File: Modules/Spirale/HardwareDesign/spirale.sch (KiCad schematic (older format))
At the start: 1 part

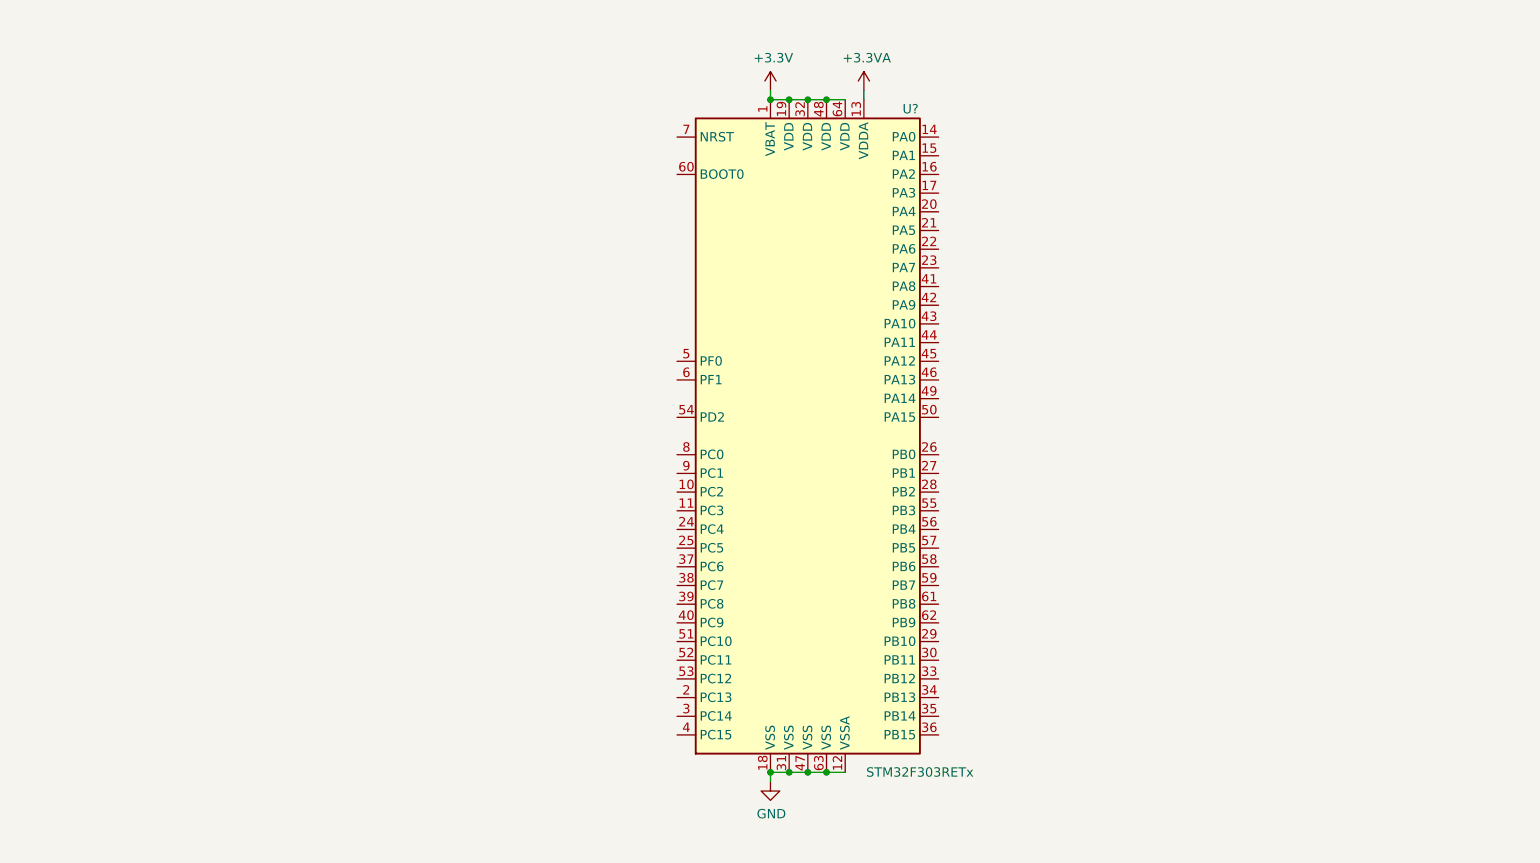
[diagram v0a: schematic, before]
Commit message: hw: add most of the needed nets
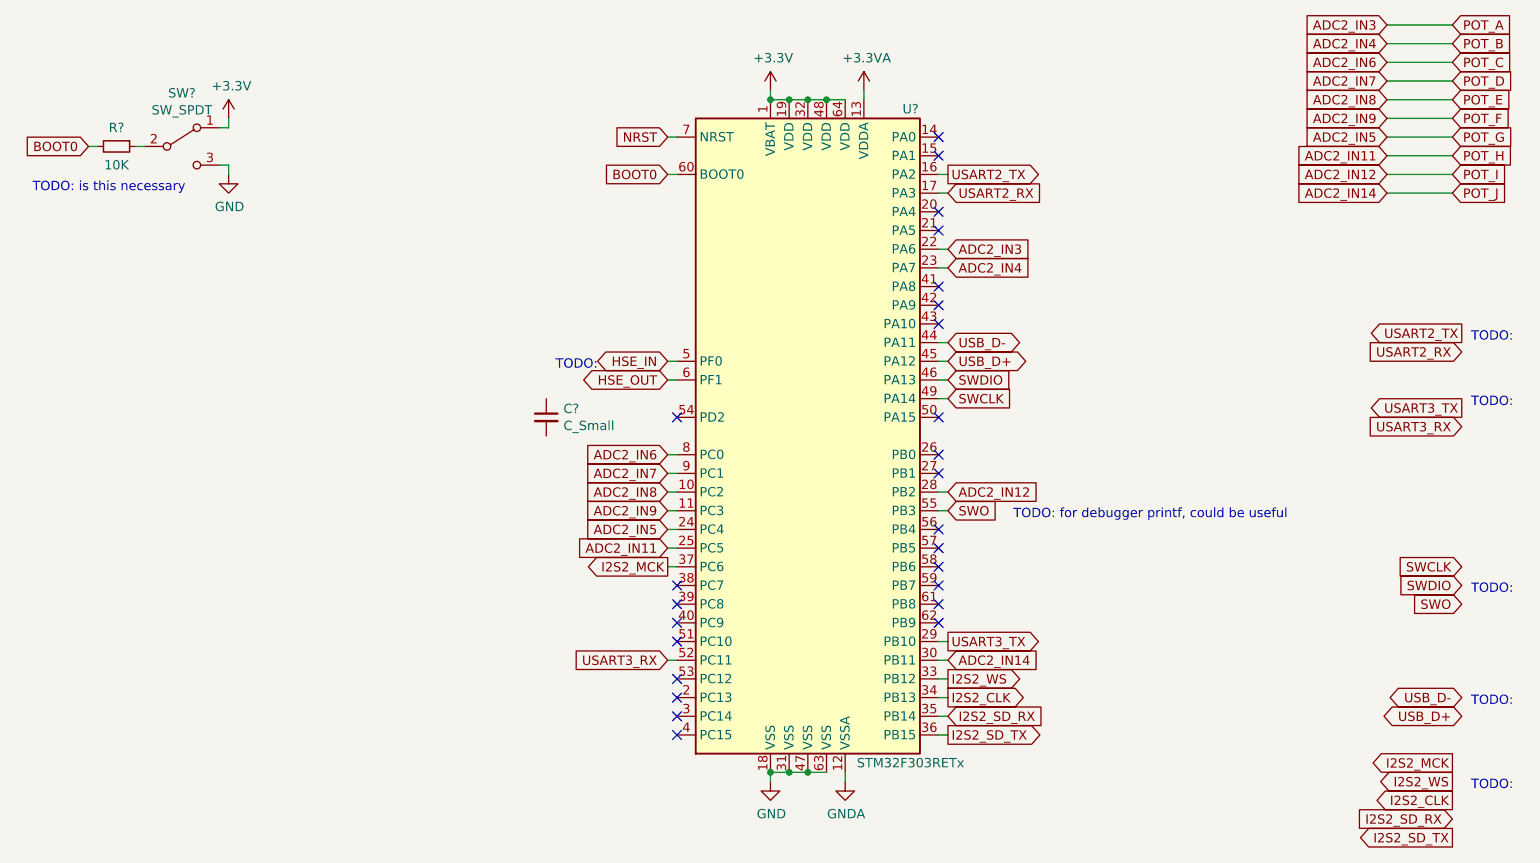
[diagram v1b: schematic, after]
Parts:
- added C?: C_Small, symbol Device:C_Small
- added R?: 10K, symbol Device:R_Small
- added SW?: SW_SPDT, symbol Switch:SW_SPDT
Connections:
- net +3V3: now also SW?.1 (A)
- net GND: now also SW?.3 (C); no longer U?.12 (VSSA)
- net ADC2_IN8: now reaches U?.10 (PC2)
- net ADC2_IN9: now reaches U?.11 (PC3)
- net USART2_TX: now reaches U?.16 (PA2)
- net USART2_RX: now reaches U?.17 (PA3)
- net ADC2_IN3: now reaches U?.22 (PA6)
- net ADC2_IN4: now reaches U?.23 (PA7)
- net ADC2_IN5: now reaches U?.24 (PC4)
- net ADC2_IN11: now reaches U?.25 (PC5)
- net ADC2_IN12: now reaches U?.28 (PB2)
- net USART3_TX: now reaches U?.29 (PB10)
- net ADC2_IN14: now reaches U?.30 (PB11)
- net I2S2_WS: now reaches U?.33 (PB12)
- net I2S2_CLK: now reaches U?.34 (PB13)
- net I2S2_SD_RX: now reaches U?.35 (PB14)
- net I2S2_SD_TX: now reaches U?.36 (PB15)
- net I2S2_MCK: now reaches U?.37 (PC6)
- net USB_D-: now reaches U?.44 (PA11)
- net USB_D+: now reaches U?.45 (PA12)
- net SWDIO: now reaches U?.46 (PA13)
- net SWCLK: now reaches U?.49 (PA14)
- net HSE_IN: now reaches U?.5 (PF0)
- net USART3_RX: now reaches U?.52 (PC11)
- net SWO: now reaches U?.55 (PB3)
- net HSE_OUT: now reaches U?.6 (PF1)
- net BOOT0: now reaches U?.60 (BOOT0)
- net BOOT0: now also R?.2
- net NRST: now reaches U?.7 (NRST)
- net ADC2_IN6: now reaches U?.8 (PC0)
- net ADC2_IN7: now reaches U?.9 (PC1)
- new net: R?.1, SW?.2 (B)
- new net GNDA: U?.12 (VSSA)
- no-connect marks 0 -> 25
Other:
- note added: "TODO: \n"
- note added: "TODO: for debugger printf, could be useful\n"
- note added: "TODO: is this necessary\n"
